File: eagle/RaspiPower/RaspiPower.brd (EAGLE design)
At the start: 50 x 33.5 mm, 31 parts, among them K1 4052

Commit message: Still fixing the board, not finished
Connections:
- net VCC: now also K1.S1, U$2.2; no longer K1.O1, U$2.1
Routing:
- net VCC: track 142.0 -> 157.5 mm
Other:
- board text added: "v1.1 - Oct 2017"
- board text removed: "v1.0 - Sept 2017"
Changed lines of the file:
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@@
 <text x="25.90881875" y="7.555653125" size="1.27" layer="21">HK4100F</text>
 <text x="42.51348125" y="7.5914625" size="1.27" layer="22" rot="MR0">electrogeek.cc/RaspiPower</text>
-<text x="35.89301875" y="5.98006875" size="0.8128" layer="22" rot="MR0">v1.0 - Sept 2017</text>
+<text x="35.89301875" y="5.98006875" size="0.8128" layer="22" rot="MR0">v1.1 - Oct 2017</text>
 <text x="45.913003125" y="12.68815625" size="1.27" layer="21">-</text>
 <text x="12.26119375" y="-0.01184375" size="1.27" layer="21">-</text>
@@
 <wire x1="6.35" y1="1.27" x2="2.54" y2="6.35" width="1.016" layer="52"/>
 <wire x1="6.35" y1="7.62" x2="7.62" y2="7.62" width="1.016" layer="52"/>
+<rectangle x1="6.492046875" y1="2.36009375" x2="8.827746875" y2="4.564446875" layer="1"/>
 </plain>
 <attributes>
@@
 <contactref element="K1" pad="1"/>
 <contactref element="D1" pad="C"/>
-<contactref element="K1" pad="O1"/>
 <contactref element="NPNOR1" pad="C"/>
 <contactref element="NPNOR2" pad="C"/>
 <contactref element="R5" pad="2"/>
 <contactref element="JSPIPROG" pad="2"/>
-<contactref element="U$2" pad="1"/>
 <contactref element="U$2" pad="11"/>
 <contactref element="JIN" pad="2"/>
@@
 <wire x1="4" y1="7.625" x2="3.995" y2="7.65" width="0.1524" layer="1"/>
 <wire x1="7.5" y1="7.875" x2="7.58" y2="7.95" width="0.1524" layer="1"/>
-<wire x1="9.5" y1="8.0575" x2="12.76" y2="5.115" width="0.4064" layer="1"/>
+<wire x1="9.023546875" y1="8.20670625" x2="12.76" y2="5.115" width="1.016" layer="1"/>
 <wire x1="12.76" y1="5.115" x2="12.625" y2="5.25" width="0.1524" layer="1"/>
-<wire x1="7.625" y1="8.0575" x2="9.5" y2="8.0575" width="0.4064" layer="1"/>
-<wire x1="7.625" y1="8" x2="7.625" y2="8.0575" width="0.1524" layer="1"/>
+<wire x1="7.148546875" y1="8.20670625" x2="9.023546875" y2="8.20670625" width="1.016" layer="1"/>
+<wire x1="7.625" y1="8" x2="7.148546875" y2="8.20670625" width="0.1524" layer="1"/>
 <wire x1="12.625" y1="5.25" x2="12.7" y2="5.207" width="0.1524" layer="1"/>
 <wire x1="7.625" y1="8" x2="7.58" y2="7.95" width="0.1524" layer="1"/>
@@
 <wire x1="2.625" y1="16.5" x2="2.54" y2="16.51" width="0.1524" layer="1"/>
 <wire x1="5.8375" y1="7.625" x2="3.995" y2="7.65" width="0.1524" layer="1"/>
-<wire x1="22.835" y1="7.01" x2="22.875" y2="3.875" width="1.016" layer="1"/>
 <wire x1="25.375" y1="11.375" x2="25.375" y2="7" width="1.016" layer="1"/>
-<wire x1="25.375" y1="7" x2="22.835" y2="7.01" width="1.016" layer="1"/>
-<wire x1="22.875" y1="3.875" x2="22.86" y2="3.81" width="0.1524" layer="1"/>
 <wire x1="25.375" y1="11.375" x2="25.4" y2="11.43" width="0.1524" layer="1"/>
-<wire x1="29.875" y1="7" x2="33" y2="3.875" width="1.016" layer="1"/>
-<wire x1="25.375" y1="7" x2="29.875" y2="7" width="1.016" layer="1"/>
-<wire x1="33" y1="3.875" x2="33.02" y2="3.81" width="0.1524" layer="1"/>
 <wire x1="22.75" y1="21.5" x2="20.5" y2="21.5" width="0.3048" layer="1"/>
 <wire x1="20.5" y1="21.5" x2="20.47875" y2="21.43125" width="0.1524" layer="1"/>
@@
 <wire x1="15.4225" y1="0.865" x2="15.24" y2="5.08" width="1.016" layer="1"/>
 <wire x1="15.24" y1="5.08" x2="12.75" y2="5.125" width="1.016" layer="1"/>
-<wire x1="22.75" y1="0.865" x2="15.4225" y2="0.865" width="1.016" layer="1"/>
-<wire x1="22.75" y1="3.75" x2="22.75" y2="0.865" width="1.016" layer="1"/>
+<wire x1="25.29" y1="0.865" x2="15.4225" y2="0.865" width="1.016" layer="1"/>
 <wire x1="12.75" y1="5.125" x2="12.7" y2="5.207" width="0.1524" layer="1"/>
-<wire x1="22.75" y1="3.75" x2="22.86" y2="3.81" width="0.1524" layer="1"/>
 <wire x1="12.7" y1="5.08" x2="7.62" y2="5.08" width="0.254" layer="16"/>
 <wire x1="7.62" y1="5.08" x2="7.62" y2="11.43" width="0.254" layer="16"/>
@@
 <wire x1="33.02" y1="19.05" x2="36.16926875" y2="21.00804375" width="0.254" layer="1"/>
 <wire x1="36.16926875" y1="21.00804375" x2="36.169065625" y2="22.96225625" width="0.254" layer="1"/>
+<contactref element="K1" pad="S1"/>
+<contactref element="U$2" pad="2"/>
+<wire x1="25.29051875" y1="0.87116875" x2="25.4" y2="3.81" width="1.016" layer="1"/>
+<wire x1="25.4" y1="3.81" x2="25.377146875" y2="7.017478125" width="1.016" layer="1"/>
+<wire x1="25.4" y1="3.81" x2="25.4161875" y2="0.857790625" width="1.016" layer="1"/>
+<wire x1="25.4161875" y1="0.857790625" x2="43.192471875" y2="0.857790625" width="1.016" layer="1"/>
+<wire x1="43.192471875" y1="0.857790625" x2="43.18" y2="3.81" width="1.016" layer="1"/>
 <wire x1="36.169065625" y1="22.96225625" x2="36.171509375" y2="22.953290625" width="0" layer="19" extent="1-1"/>
+<wire x1="25.377146875" y1="7.017478125" x2="25.375" y2="7" width="0" layer="19" extent="1-1"/>
+<wire x1="25.29" y1="0.865" x2="25.29051875" y2="0.87116875" width="0" layer="19" extent="1-1"/>
 <wire x1="12.7" y1="5.08" x2="12.75" y2="5.125" width="0" layer="19" extent="1-16"/>
 </signal>

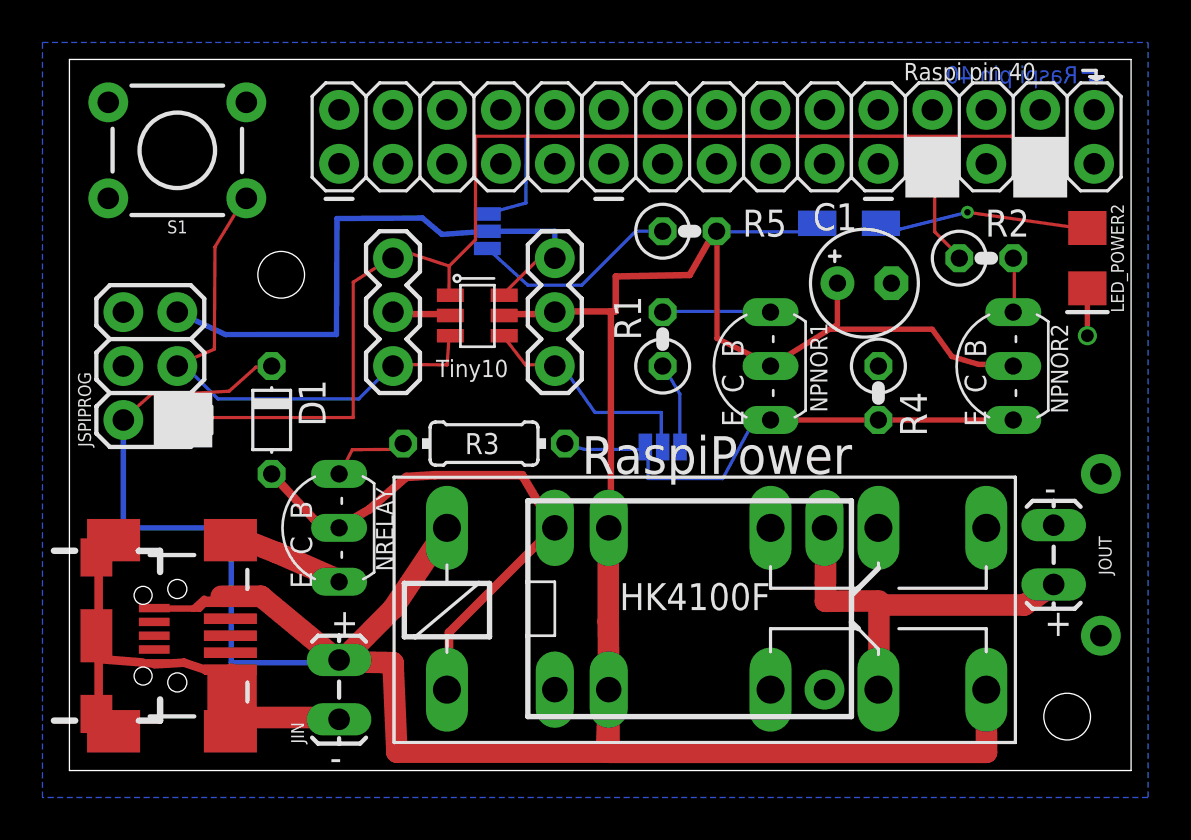
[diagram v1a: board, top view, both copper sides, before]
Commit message: Added HK4100F relay part to library, and v1.2 of the RaspiPower
Conclusion: don't use other third party parts symbols found on the net
without verifying thoroughly that their are good.
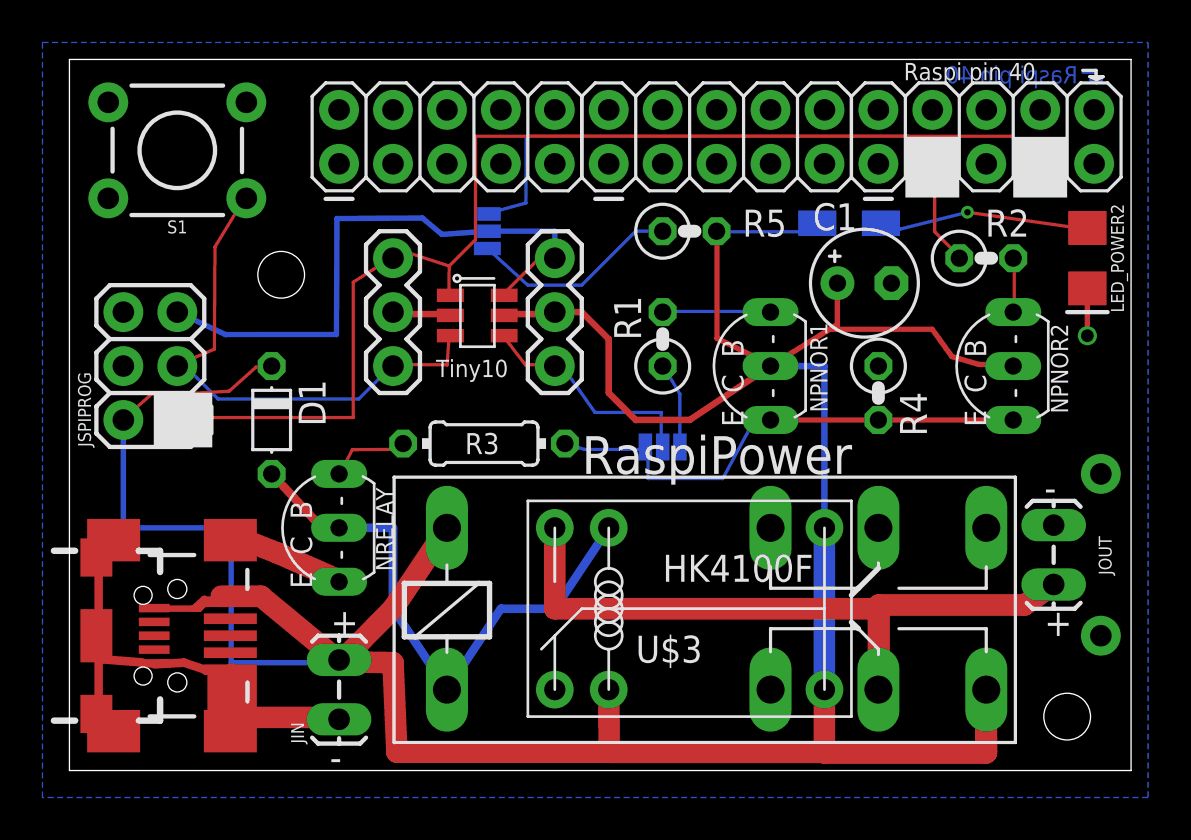
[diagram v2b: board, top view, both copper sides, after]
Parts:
- removed J9: (no value), SparkFun-Connectors:1X01_NO_SILK
- removed U$2: HK4100F-DC5V, huike:SMR1
- added U$3: HK4100F, kalshagar:HK4100F
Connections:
- removed net N$3: JOUT.1, K1.P1, U$2.7
- new net VOUT: JOUT.1, K1.P1, U$3.P$6
- net N$9: now also U$3.P$5; no longer U$2.12
- net VCC: now also U$3.P$2, U$3.P$3, U$3.P$4; no longer U$2.11, U$2.2
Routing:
- net VOUT: track 0.00 -> 35.6 mm
- net N$3: track 18.7 -> 0.00 mm
- net VCC: track 157.5 -> 172.1 mm
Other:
- board text added: "v1.2 - Oct 2017"
- board text removed: "HK4100F"
- board text removed: "v1.1 - Oct 2017"
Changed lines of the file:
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@@
 <text x="45.913003125" y="6.33815625" size="1.27" layer="21">+</text>
 <rectangle x1="3.972209375" y1="15.218734375" x2="6.727703125" y2="17.796965625" layer="21"/>
-<text x="25.90881875" y="7.555653125" size="1.27" layer="21">HK4100F</text>
 <text x="42.51348125" y="7.5914625" size="1.27" layer="22" rot="MR0">electrogeek.cc/RaspiPower</text>
-<text x="35.89301875" y="5.98006875" size="0.8128" layer="22" rot="MR0">v1.1 - Oct 2017</text>
+<text x="35.89301875" y="5.98006875" size="0.8128" layer="22" rot="MR0">v1.2 - Oct 2017</text>
 <text x="45.913003125" y="12.68815625" size="1.27" layer="21">-</text>
 <text x="12.26119375" y="-0.01184375" size="1.27" layer="21">-</text>
@@
 </element>
 <element name="JSPIPROG" library="SparkFun-Connectors" package="2X3" value="AVR_SPI_PROG_3X2PTH" x="5.08" y="16.51" rot="R90"/>
-<element name="U$2" library="huike" package="SMR1" value="HK4100F-DC5V" x="29.21" y="7.62" smashed="yes">
-<attribute name="VALUE" x="38.98" y="5.08" size="1.27" layer="27" rot="R90"/>
-</element>
 <element name="JOUT" library="SparkFun-Connectors" package="1X02_LOCK_LONGPADS" value="" x="46.355" y="8.89" smashed="yes" rot="R90">
 <attribute name="NAME" x="49.084696875" y="9.21005" size="0.6096" layer="25" font="vector" ratio="20" rot="R90"/>
@@
 <attribute name="VALUE" x="11.43" y="26.035" size="0.6096" layer="27" font="vector" ratio="20"/>
 </element>
-<element name="J9" library="SparkFun-Connectors" package="1X01_NO_SILK" value="" x="35.56" y="3.81" smashed="yes">
-<attribute name="VALUE" x="34.29" y="2.032" size="0.6096" layer="27" font="vector" ratio="20"/>
-</element>
 <element name="R6" library="resistor" package="R1206W" value="1k" x="36.716175" y="25.7728625" smashed="yes" rot="MR0">
 <attribute name="NAME" x="34.8633375" y="23.432584375" size="1.27" layer="26" rot="MR0"/>
@@
 <attribute name="VALUE" x="39.854509375" y="20.540290625" size="1.27" layer="27" ratio="10"/>
 </element>
+<element name="U$3" library="kalshagar" package="HK4100F" value="HK4100F" x="26.67" y="6.35"/>
 </elements>
 <signals>
@@
 <contactref element="R5" pad="2"/>
 <contactref element="JSPIPROG" pad="2"/>
-<contactref element="U$2" pad="11"/>
 <contactref element="JIN" pad="2"/>
 <contactref element="R6" pad="2"/>
@@
 <wire x1="2.625" y1="16.5" x2="2.54" y2="16.51" width="0.1524" layer="1"/>
 <wire x1="5.8375" y1="7.625" x2="3.995" y2="7.65" width="0.1524" layer="1"/>
-<wire x1="25.375" y1="11.375" x2="25.375" y2="7" width="1.016" layer="1"/>
-<wire x1="25.375" y1="11.375" x2="25.4" y2="11.43" width="0.1524" layer="1"/>
 <wire x1="22.75" y1="21.5" x2="20.5" y2="21.5" width="0.3048" layer="1"/>
 <wire x1="20.5" y1="21.5" x2="20.47875" y2="21.43125" width="0.1524" layer="1"/>
@@
 <wire x1="44.375" y1="19.125" x2="44.45" y2="19.05" width="0.1524" layer="1"/>
 <wire x1="33.125" y1="19.125" x2="33.02" y2="19.05" width="0.1524" layer="1"/>
-<wire x1="25.73" y1="21.625" x2="25.5" y2="21.625" width="0.3048" layer="1"/>
-<wire x1="25.5" y1="21.625" x2="22.875" y2="21.625" width="0.3048" layer="1"/>
-<wire x1="25.73" y1="23.27" x2="25.73" y2="21.625" width="0.3048" layer="1"/>
-<wire x1="30.375" y1="25.375" x2="29.21" y2="23.33625" width="0.3048" layer="1"/>
-<wire x1="29.21" y1="23.33625" x2="25.73" y2="23.27" width="0.3048" layer="1"/>
-<wire x1="22.875" y1="21.625" x2="22.86" y2="21.59" width="0.1524" layer="1"/>
-<wire x1="30.375" y1="25.375" x2="30.48" y2="25.4" width="0.1524" layer="1"/>
-<wire x1="25.5" y1="21.625" x2="25.5" y2="11.5" width="0.3048" layer="1"/>
-<wire x1="25.5" y1="11.5" x2="25.4" y2="11.43" width="0.1524" layer="1"/>
 <wire x1="15.4225" y1="0.865" x2="15.24" y2="5.08" width="1.016" layer="1"/>
 <wire x1="15.24" y1="5.08" x2="12.75" y2="5.125" width="1.016" layer="1"/>
@@
 <wire x1="36.16926875" y1="21.00804375" x2="36.169065625" y2="22.96225625" width="0.254" layer="1"/>
 <contactref element="K1" pad="S1"/>
-<contactref element="U$2" pad="2"/>
-<wire x1="25.29051875" y1="0.87116875" x2="25.4" y2="3.81" width="1.016" layer="1"/>
-<wire x1="25.4" y1="3.81" x2="25.377146875" y2="7.017478125" width="1.016" layer="1"/>
-<wire x1="25.4" y1="3.81" x2="25.4161875" y2="0.857790625" width="1.016" layer="1"/>
 <wire x1="25.4161875" y1="0.857790625" x2="43.192471875" y2="0.857790625" width="1.016" layer="1"/>
 <wire x1="43.192471875" y1="0.857790625" x2="43.18" y2="3.81" width="1.016" layer="1"/>
+<contactref element="U$3" pad="P$2"/>
+<contactref element="U$3" pad="P$4"/>
+<contactref element="U$3" pad="P$3"/>
+<wire x1="25.4" y1="3.81" x2="25.422465625" y2="0.864171875" width="1.016" layer="1"/>
+<wire x1="43.18" y1="3.81" x2="43.173490625" y2="0.828565625" width="1.016" layer="1"/>
+<wire x1="43.173490625" y1="0.828565625" x2="35.553421875" y2="0.828565625" width="1.016" layer="1"/>
+<wire x1="35.553421875" y1="0.828565625" x2="35.56" y2="3.81" width="1.016" layer="1"/>
+<wire x1="35.56" y1="3.81" x2="35.56" y2="11.43" width="1.016" layer="16"/>
+<wire x1="35.56" y1="11.43" x2="35.56" y2="19.05" width="0.3048" layer="16"/>
+<wire x1="35.56" y1="19.05" x2="33.02" y2="19.05" width="0.3048" layer="16"/>
+<wire x1="33.02" y1="19.05" x2="29.21" y2="16.51" width="0.3048" layer="1"/>
+<wire x1="29.21" y1="16.51" x2="26.67" y2="16.51" width="0.3048" layer="1"/>
+<wire x1="26.67" y1="16.51" x2="25.4" y2="17.78" width="0.3048" layer="1"/>
+<wire x1="25.4" y1="17.78" x2="25.4" y2="20.32" width="0.3048" layer="1"/>
+<wire x1="25.4" y1="20.32" x2="24.13" y2="21.59" width="0.3048" layer="1"/>
+<wire x1="24.13" y1="21.59" x2="22.86" y2="21.59" width="0.3048" layer="1"/>
 <wire x1="36.169065625" y1="22.96225625" x2="36.171509375" y2="22.953290625" width="0" layer="19" extent="1-1"/>
-<wire x1="25.377146875" y1="7.017478125" x2="25.375" y2="7" width="0" layer="19" extent="1-1"/>
-<wire x1="25.29" y1="0.865" x2="25.29051875" y2="0.87116875" width="0" layer="19" extent="1-1"/>
+<wire x1="25.422465625" y1="0.864171875" x2="25.4161875" y2="0.857790625" width="0" layer="19" extent="1-1"/>
+<wire x1="25.29" y1="0.865" x2="25.4161875" y2="0.857790625" width="0" layer="19" extent="1-1"/>
 <wire x1="12.7" y1="5.08" x2="12.75" y2="5.125" width="0" layer="19" extent="1-16"/>
 </signal>
@@
 <contactref element="NRELAY" pad="C"/>
 <contactref element="D1" pad="A"/>
-<contactref element="U$2" pad="12"/>
 <wire x1="11.53" y1="11.8175" x2="12.625" y2="11.5" width="0.4064" layer="1"/>
 <wire x1="9.625" y1="13.875" x2="11.53" y2="11.8175" width="0.4064" layer="1"/>
 <wire x1="12.625" y1="11.5" x2="12.7" y2="11.43" width="0.1524" layer="1"/>
 <wire x1="9.625" y1="13.875" x2="9.525" y2="13.97" width="0.1524" layer="1"/>
-<wire x1="17.875" y1="6.5" x2="22.75" y2="11.375" width="0.4064" layer="1"/>
-<wire x1="17.875" y1="3.875" x2="17.875" y2="6.5" width="0.4064" layer="1"/>
-<wire x1="22.75" y1="11.375" x2="22.86" y2="11.43" width="0.1524" layer="1"/>
-<wire x1="17.875" y1="3.875" x2="17.78" y2="3.81" width="0.1524" layer="1"/>
-<wire x1="14.11875" y1="12.29375" x2="12.75" y2="11.5" width="0.4064" layer="1"/>
-<wire x1="15.865" y1="13.8275" x2="14.11875" y2="12.29375" width="0.4064" layer="1"/>
-<wire x1="17.21625" y1="13.90875" x2="15.865" y2="13.8275" width="0.4064" layer="1"/>
-<wire x1="21.32125" y1="13.90875" x2="17.21625" y2="13.90875" width="0.4064" layer="1"/>
-<wire x1="22.75" y1="11.5" x2="21.32125" y2="13.90875" width="0.4064" layer="1"/>
-<wire x1="12.75" y1="11.5" x2="12.7" y2="11.43" width="0.1524" layer="1"/>
-<wire x1="22.75" y1="11.5" x2="22.86" y2="11.43" width="0.1524" layer="1"/>
-</signal>
-<signal name="N$3">
+<contactref element="U$3" pad="P$5"/>
+<wire x1="12.7" y1="11.43" x2="15.24" y2="11.43" width="0.4064" layer="16"/>
+<wire x1="15.24" y1="11.43" x2="15.24" y2="7.62" width="0.4064" layer="16"/>
+<wire x1="15.24" y1="7.62" x2="17.78" y2="3.81" width="0.4064" layer="16"/>
+<wire x1="17.78" y1="3.81" x2="20.32" y2="7.62" width="0.4064" layer="16"/>
+<wire x1="20.32" y1="7.62" x2="22.86" y2="7.62" width="0.4064" layer="16"/>
+<wire x1="22.86" y1="7.62" x2="25.4" y2="11.43" width="0.4064" layer="16"/>
+</signal>
+<signal name="VOUT">
 <contactref element="K1" pad="P1"/>
-<contactref element="U$2" pad="7"/>
 <contactref element="JOUT" pad="1"/>
 <wire x1="38.125" y1="7.7975" x2="44.98" y2="7.7975" width="1.016" layer="1"/>
@@
 <wire x1="44.98" y1="7.7975" x2="46.355" y2="8.763" width="1.016" layer="1"/>
 <wire x1="38.125" y1="3.875" x2="38.1" y2="3.81" width="0.1524" layer="1"/>
-<wire x1="35.605" y1="8.855" x2="35.625" y2="11.375" width="1.016" layer="1"/>
-<wire x1="35.605" y1="7.97" x2="35.605" y2="8.855" width="1.016" layer="1"/>
-<wire x1="38.125" y1="7.99" x2="35.605" y2="7.97" width="1.016" layer="1"/>
-<wire x1="35.625" y1="11.375" x2="35.56" y2="11.43" width="0.1524" layer="1"/>
+<contactref element="U$3" pad="P$6"/>
+<wire x1="38.1" y1="3.81" x2="38.1" y2="7.62" width="1.016" layer="1"/>
+<wire x1="38.1" y1="7.62" x2="22.86" y2="7.62" width="1.016" layer="1"/>
+<wire x1="22.86" y1="7.62" x2="22.86" y2="11.43" width="1.016" layer="1"/>
 </signal>
 <signal name="N$4">
